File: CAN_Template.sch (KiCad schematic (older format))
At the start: 21 parts, among them U5 SN74LVC1T45DBVR, U6 SN65HVD1050D, U7 MCP2515-xSO, U8 SN74LVC1T45DBVR

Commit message: A very rough placement of components, some routing
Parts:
- removed D3: D5V0L2B3W-7, Package_TO_SOT_SMD:SOT-23, symbol Device:D_TVS_x2_CAA
- added D3: D_TVS_x2_AAC, Package_TO_SOT_SMD:SOT-23, symbol Device:D_TVS_x2_AAC
- C18, C19, C20, C21, C22, C23, C24, C25, C50, C51: footprint Capacitor_SMD:C_0805_2012Metric -> Capacitor_SMD:C_0603_1608Metric
- NP1, NP2, R12, R13, R14, R15: footprint Resistor_SMD:R_0805_2012Metric -> Resistor_SMD:R_0603_1608Metric
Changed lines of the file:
@@
 F 0 "NP1" H 8668 3446 50  0000 L CNN
 F 1 "60" H 8668 3355 50  0000 L CNN
-F 2 "Resistor_SMD:R_0805_2012Metric" V 8640 3390 50  0001 C CNN
+F 2 "Resistor_SMD:R_0603_1608Metric" V 8640 3390 50  0001 C CNN
 F 3 "~" H 8600 3400 50  0001 C CNN
 	1    8600 3400
@@
 F 0 "C19" V 7498 2850 50  0000 C CNN
 F 1 "1nf" V 7589 2850 50  0000 C CNN
-F 2 "Capacitor_SMD:C_0805_2012Metric" H 7788 2700 50  0001 C CNN
+F 2 "Capacitor_SMD:C_0603_1608Metric" H 7788 2700 50  0001 C CNN
 F 3 "~" H 7750 2850 50  0001 C CNN
 	1    7750 2850
@@
 F 0 "C21" V 7650 2850 50  0000 C CNN
 F 1 "100nf" V 7589 3050 50  0000 C CNN
-F 2 "Capacitor_SMD:C_0805_2012Metric" H 7788 2900 50  0001 C CNN
+F 2 "Capacitor_SMD:C_0603_1608Metric" H 7788 2900 50  0001 C CNN
 F 3 "~" H 7750 3050 50  0001 C CNN
 	1    7750 3050
@@
 F 0 "C24" H 8715 4346 50  0000 L CNN
 F 1 "100pf" H 8715 4255 50  0000 L CNN
-F 2 "Capacitor_SMD:C_0805_2012Metric" H 8638 4150 50  0001 C CNN
+F 2 "Capacitor_SMD:C_0603_1608Metric" H 8638 4150 50  0001 C CNN
 F 3 "~" H 8600 4300 50  0001 C CNN
 	1    8600 4300
@@
 F 0 "NP2" H 8668 3846 50  0000 L CNN
 F 1 "60" H 8668 3755 50  0000 L CNN
-F 2 "Resistor_SMD:R_0805_2012Metric" V 8640 3790 50  0001 C CNN
+F 2 "Resistor_SMD:R_0603_1608Metric" V 8640 3790 50  0001 C CNN
 F 3 "~" H 8600 3800 50  0001 C CNN
 	1    8600 3800
@@
 F 0 "C23" H 9015 3646 50  0000 L CNN
 F 1 "1nf" H 9015 3555 50  0000 L CNN
-F 2 "Capacitor_SMD:C_0805_2012Metric" H 8938 3450 50  0001 C CNN
+F 2 "Capacitor_SMD:C_0603_1608Metric" H 8938 3450 50  0001 C CNN
 F 3 "~" H 8900 3600 50  0001 C CNN
 	1    8900 3600
@@
 F 0 "R13" H 8368 3646 50  0000 L CNN
 F 1 "0" H 8368 3555 50  0000 L CNN
-F 2 "Resistor_SMD:R_0805_2012Metric" V 8340 3590 50  0001 C CNN
+F 2 "Resistor_SMD:R_0603_1608Metric" V 8340 3590 50  0001 C CNN
 F 3 "~" H 8300 3600 50  0001 C CNN
 	1    8300 3600
 	0    -1   -1   0
-$EndComp
-$Comp
-L Device:D_TVS_x2_CAA D3
-U 1 1 5DD0169A
-P 9350 3600
-F 0 "D3" V 9304 3679 50  0000 L CNN
-F 1 "D5V0L2B3W-7" V 9395 3679 50  0000 L CNN
-F 2 "Package_TO_SOT_SMD:SOT-23" H 9200 3600 50  0001 C CNN
-F 3 "https://www.mouser.com/datasheet/2/115/D5V0L2B3W-218988.pdf" H 9200 3600 50  0001 C CNN
-	1    9350 3600
-	0    1    1    0
 $EndComp
 $Comp
@@
 F 0 "R14" H 6918 4096 50  0000 L CNN
 F 1 "10k" H 6918 4005 50  0000 L CNN
-F 2 "Resistor_SMD:R_0805_2012Metric" V 6890 4040 50  0001 C CNN
+F 2 "Resistor_SMD:R_0603_1608Metric" V 6890 4040 50  0001 C CNN
 F 3 "~" H 6850 4050 50  0001 C CNN
 	1    6850 4050
@@
 F 0 "R12" H 3918 2996 50  0000 L CNN
 F 1 "0" H 3918 2905 50  0000 L CNN
-F 2 "Resistor_SMD:R_0805_2012Metric" V 3890 2940 50  0001 C CNN
+F 2 "Resistor_SMD:R_0603_1608Metric" V 3890 2940 50  0001 C CNN
 F 3 "~" H 3850 2950 50  0001 C CNN
 	1    3850 2950
@@
 F 0 "C20" H 8715 2946 50  0000 L CNN
 F 1 "100pf" H 8715 2855 50  0000 L CNN
-F 2 "Capacitor_SMD:C_0805_2012Metric" H 8638 2750 50  0001 C CNN
+F 2 "Capacitor_SMD:C_0603_1608Metric" H 8638 2750 50  0001 C CNN
 F 3 "~" H 8600 2900 50  0001 C CNN
 	1    8600 2900
@@
 F 0 "C51" V 2248 5000 50  0000 C CNN
 F 1 "1nf" V 2339 5000 50  0000 C CNN
-F 2 "Capacitor_SMD:C_0805_2012Metric" H 2538 4850 50  0001 C CNN
+F 2 "Capacitor_SMD:C_0603_1608Metric" H 2538 4850 50  0001 C CNN
 F 3 "~" H 2500 5000 50  0001 C CNN
 	1    2500 5000
@@
 F 0 "C50" V 2400 4600 50  0000 C CNN
 F 1 "100nf" V 2339 4800 50  0000 C CNN
-F 2 "Capacitor_SMD:C_0805_2012Metric" H 2538 4650 50  0001 C CNN
+F 2 "Capacitor_SMD:C_0603_1608Metric" H 2538 4650 50  0001 C CNN
 F 3 "~" H 2500 4800 50  0001 C CNN
 	1    2500 4800
@@
 F 0 "C18" V 4300 2800 50  0000 C CNN
 F 1 "100pf" V 3989 2800 50  0000 C CNN
-F 2 "Capacitor_SMD:C_0805_2012Metric" H 4188 2650 50  0001 C CNN
+F 2 "Capacitor_SMD:C_0603_1608Metric" H 4188 2650 50  0001 C CNN
 F 3 "~" H 4150 2800 50  0001 C CNN
 	1    4150 2800
@@
 F 0 "C22" H 6892 3196 50  0000 L CNN
 F 1 "100pF" H 6892 3105 50  0000 L CNN
-F 2 "Capacitor_SMD:C_0805_2012Metric" H 6800 3150 50  0001 C CNN
+F 2 "Capacitor_SMD:C_0603_1608Metric" H 6800 3150 50  0001 C CNN
 F 3 "~" H 6800 3150 50  0001 C CNN
 	1    6800 3150
@@
 F 0 "C25" V 5900 4450 50  0000 C CNN
 F 1 "100pf" V 5589 4450 50  0000 C CNN
-F 2 "Capacitor_SMD:C_0805_2012Metric" H 5788 4300 50  0001 C CNN
+F 2 "Capacitor_SMD:C_0603_1608Metric" H 5788 4300 50  0001 C CNN
 F 3 "~" H 5750 4450 50  0001 C CNN
 	1    5750 4450
@@
 F 0 "R15" H 6118 4346 50  0000 L CNN
 F 1 "0" H 6118 4255 50  0000 L CNN
-F 2 "Resistor_SMD:R_0805_2012Metric" V 6090 4290 50  0001 C CNN
+F 2 "Resistor_SMD:R_0603_1608Metric" V 6090 4290 50  0001 C CNN
 F 3 "~" H 6050 4300 50  0001 C CNN
 	1    6050 4300
@@
 	-1   0    0    1
 $EndComp
+$Comp
+L Device:D_TVS_x2_AAC D3
+U 1 1 5E29CE34
+P 9350 3600
+F 0 "D3" V 9304 3679 50  0000 L CNN
+F 1 "D_TVS_x2_AAC" V 9395 3679 50  0000 L CNN
+F 2 "Package_TO_SOT_SMD:SOT-23" H 9200 3600 50  0001 C CNN
+F 3 "~" H 9200 3600 50  0001 C CNN
+	1    9350 3600
+	0    1    1    0
+$EndComp
 $EndSCHEMATC

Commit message: Fixed caps and added grounding
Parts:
- U5, U8: symbol dk_Logic-Translators-Level-Shifters:SN74LVC1T45DBVR -> MASA-Radio-Board-rescue:SN74LVC1T45DBVR-dk_Logic-Translators-Level-Shifters
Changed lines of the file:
@@
 EESchema Schematic File Version 4
+LIBS:MASA-Radio Board-cache
 EELAYER 30 0
 EELAYER END
@@
 	6800 3050 6800 2950
 $Comp
-L dk_Logic-Translators-Level-Shifters:SN74LVC1T45DBVR U5
+L MASA-Radio-Board-rescue:SN74LVC1T45DBVR-dk_Logic-Translators-Level-Shifters U5
 U 1 1 5E23BA35
 P 5250 2950
+AR Path="/5E23BA35" Ref="U5"  Part="1"
+AR Path="/5E22EDDC/5E23BA35" Ref="U5"  Part="1"
 F 0 "U5" H 5250 2347 60  0000 C CNN
 F 1 "SN74LVC1T45DBVR" H 5250 2453 60  0000 C CNN
@@
 $EndComp
 $Comp
-L dk_Logic-Translators-Level-Shifters:SN74LVC1T45DBVR U8
+L MASA-Radio-Board-rescue:SN74LVC1T45DBVR-dk_Logic-Translators-Level-Shifters U8
 U 1 1 5E2400EF
 P 5250 4300
+AR Path="/5E2400EF" Ref="U8"  Part="1"
+AR Path="/5E22EDDC/5E2400EF" Ref="U8"  Part="1"
 F 0 "U8" H 5250 3697 60  0000 C CNN
 F 1 "SN74LVC1T45DBVR" H 5250 3803 60  0000 C CNN

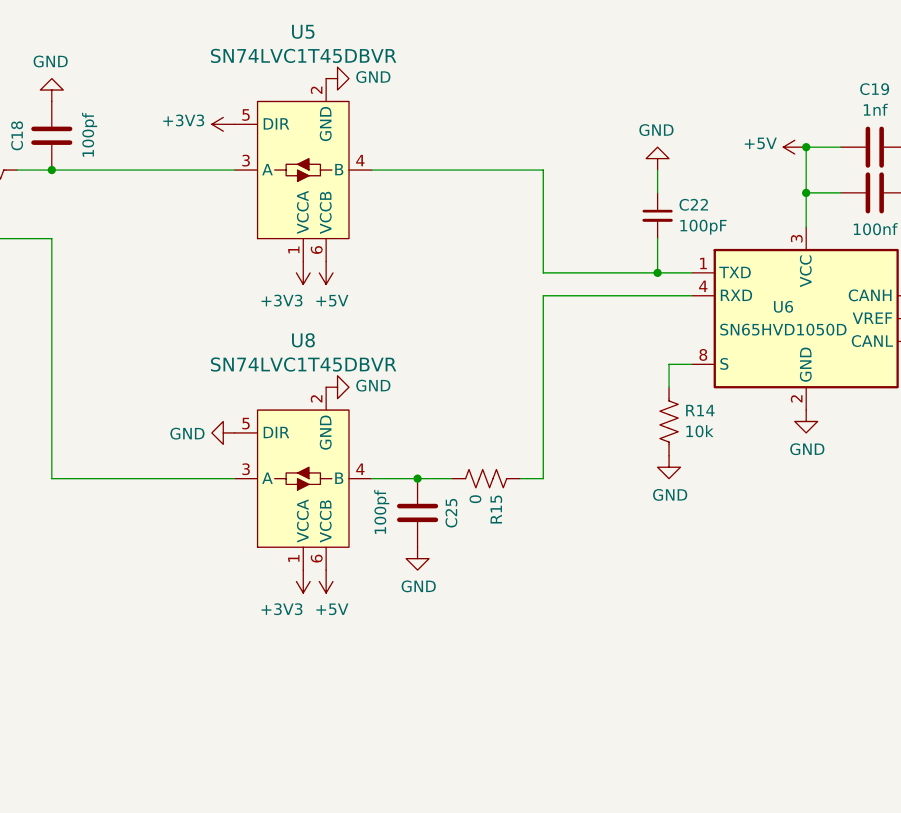
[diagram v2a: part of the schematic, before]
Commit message: Added filters and connected missing analog lines. Also fixed USB
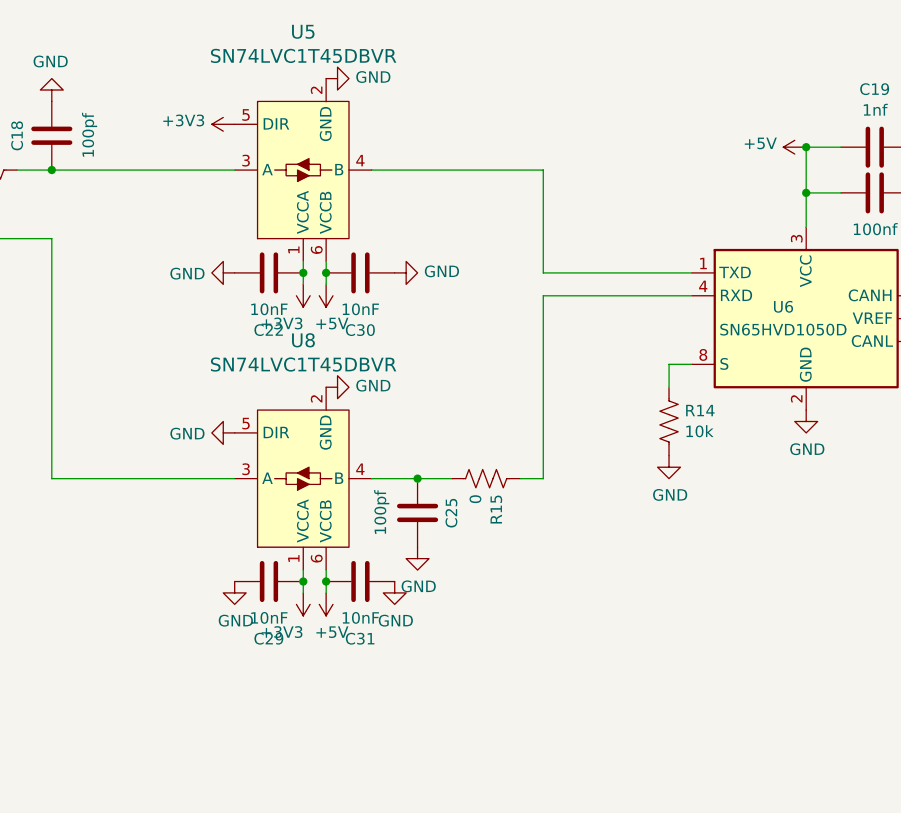
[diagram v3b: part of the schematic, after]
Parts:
- removed C22: 100pF, Capacitor_SMD:C_0603_1608Metric, symbol Device:C_Small
- added C22, C29, C30, C31: 10nF, Capacitor_SMD:C_0603_1608Metric, symbol Device:C
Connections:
- net +3V3: now also C22.2, C29.2
- net +5V: now also C30.1, C31.1
- net GND: now also C22.1, C29.1, C30.2, C31.2
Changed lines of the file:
@@
 CAN_Transciever
-$Comp
-L Device:C_Small C22
-U 1 1 5E22EBAC
-P 6800 3150
-F 0 "C22" H 6892 3196 50  0000 L CNN
-F 1 "100pF" H 6892 3105 50  0000 L CNN
-F 2 "Capacitor_SMD:C_0603_1608Metric" H 6800 3150 50  0001 C CNN
-F 3 "~" H 6800 3150 50  0001 C CNN
-	1    6800 3150
-	1    0    0    -1
-$EndComp
-Wire Wire Line
-	6950 3400 6800 3400
-Wire Wire Line
-	6800 3400 6800 3250
-$Comp
-L power:GND #PWR056
-U 1 1 5E231658
-P 6800 2950
-F 0 "#PWR056" H 6800 2700 50  0001 C CNN
-F 1 "GND" H 6805 2777 50  0000 C CNN
-F 2 "" H 6800 2950 50  0001 C CNN
-F 3 "" H 6800 2950 50  0001 C CNN
-	1    6800 2950
-	-1   0    0    1
-$EndComp
-Wire Wire Line
-	6800 3050 6800 2950
 $Comp
 L MASA-Radio-Board-rescue:SN74LVC1T45DBVR-dk_Logic-Translators-Level-Shifters U5
@@
 	0    -1   -1   0
 $EndComp
-Wire Wire Line
-	6800 3400 6300 3400
-Connection ~ 6800 3400
 $Comp
 L power:+3V3 #PWR052
@@
 L power:+3V3 #PWR059
 U 1 1 5E266276
-P 5250 3350
-F 0 "#PWR059" H 5250 3200 50  0001 C CNN
-F 1 "+3V3" H 5344 3523 50  0000 C CNN
-F 2 "" H 5250 3350 50  0001 C CNN
-F 3 "" H 5250 3350 50  0001 C CNN
-	1    5250 3350
+P 5250 3450
+F 0 "#PWR059" H 5250 3300 50  0001 C CNN
+F 1 "+3V3" H 5344 3623 50  0000 C CNN
+F 2 "" H 5250 3450 50  0001 C CNN
+F 3 "" H 5250 3450 50  0001 C CNN
+	1    5250 3450
 	-1   0    0    1
 $EndComp
@@
 L power:+5V #PWR060
 U 1 1 5E2667FA
-P 5350 3350
-F 0 "#PWR060" H 5350 3200 50  0001 C CNN
-F 1 "+5V" H 5326 3523 50  0000 C CNN
-F 2 "" H 5350 3350 50  0001 C CNN
-F 3 "" H 5350 3350 50  0001 C CNN
-	1    5350 3350
+P 5350 3450
+F 0 "#PWR060" H 5350 3300 50  0001 C CNN
+F 1 "+5V" H 5326 3623 50  0000 C CNN
+F 2 "" H 5350 3450 50  0001 C CNN
+F 3 "" H 5350 3450 50  0001 C CNN
+	1    5350 3450
 	-1   0    0    1
 $EndComp
@@
 L power:+5V #PWR069
 U 1 1 5E267CFB
-P 5350 4700
-F 0 "#PWR069" H 5350 4550 50  0001 C CNN
-F 1 "+5V" H 5326 4873 50  0000 C CNN
-F 2 "" H 5350 4700 50  0001 C CNN
-F 3 "" H 5350 4700 50  0001 C CNN
-	1    5350 4700
+P 5350 4800
+F 0 "#PWR069" H 5350 4650 50  0001 C CNN
+F 1 "+5V" H 5326 4973 50  0000 C CNN
+F 2 "" H 5350 4800 50  0001 C CNN
+F 3 "" H 5350 4800 50  0001 C CNN
+	1    5350 4800
 	-1   0    0    1
 $EndComp
@@
 L power:+3V3 #PWR068
 U 1 1 5E267CF5
-P 5250 4700
-F 0 "#PWR068" H 5250 4550 50  0001 C CNN
-F 1 "+3V3" H 5344 4873 50  0000 C CNN
-F 2 "" H 5250 4700 50  0001 C CNN
-F 3 "" H 5250 4700 50  0001 C CNN
-	1    5250 4700
+P 5250 4800
+F 0 "#PWR068" H 5250 4650 50  0001 C CNN
+F 1 "+3V3" H 5344 4973 50  0000 C CNN
+F 2 "" H 5250 4800 50  0001 C CNN
+F 3 "" H 5250 4800 50  0001 C CNN
+	1    5250 4800
 	-1   0    0    1
 $EndComp
@@
 	0    1    1    0
 $EndComp
+$Comp
+L Device:C C22
+U 1 1 5E2F1379
+P 5100 3400
+F 0 "C22" V 4848 3400 50  0000 C CNN
+F 1 "10nF" V 4939 3400 50  0000 C CNN
+F 2 "Capacitor_SMD:C_0603_1608Metric" H 5138 3250 50  0001 C CNN
+F 3 "~" H 5100 3400 50  0001 C CNN
+	1    5100 3400
+	0    -1   -1   0
+$EndComp
+$Comp
+L power:GND #PWR0102
+U 1 1 5E2F2685
+P 4950 3400
+F 0 "#PWR0102" H 4950 3150 50  0001 C CNN
+F 1 "GND" V 4955 3272 50  0000 R CNN
+F 2 "" H 4950 3400 50  0001 C CNN
+F 3 "" H 4950 3400 50  0001 C CNN
+	1    4950 3400
+	0    1    1    0
+$EndComp
+$Comp
+L Device:C C30
+U 1 1 5E2F2CA8
+P 5500 3400
+F 0 "C30" V 5248 3400 50  0000 C CNN
+F 1 "10nF" V 5339 3400 50  0000 C CNN
+F 2 "Capacitor_SMD:C_0603_1608Metric" H 5538 3250 50  0001 C CNN
+F 3 "~" H 5500 3400 50  0001 C CNN
+	1    5500 3400
+	0    -1   -1   0
+$EndComp
+$Comp
+L power:GND #PWR0103
+U 1 1 5E2F3088
+P 5650 3400
+F 0 "#PWR0103" H 5650 3150 50  0001 C CNN
+F 1 "GND" V 5655 3272 50  0000 R CNN
+F 2 "" H 5650 3400 50  0001 C CNN
+F 3 "" H 5650 3400 50  0001 C CNN
+	1    5650 3400
+	0    -1   -1   0
+$EndComp
+Wire Wire Line
+	5350 3350 5350 3400
+Connection ~ 5350 3400
+Wire Wire Line
+	5350 3400 5350 3450
+Wire Wire Line
+	5250 3450 5250 3400
+Connection ~ 5250 3400
+Wire Wire Line
+	5250 3400 5250 3350
+$Comp
+L Device:C C29
+U 1 1 5E2F68DA
+P 5100 4750
+F 0 "C29" V 4848 4750 50  0000 C CNN
+F 1 "10nF" V 4939 4750 50  0000 C CNN
+F 2 "Capacitor_SMD:C_0603_1608Metric" H 5138 4600 50  0001 C CNN
+F 3 "~" H 5100 4750 50  0001 C CNN
+	1    5100 4750
+	0    -1   -1   0
+$EndComp
+$Comp
+L Device:C C31
+U 1 1 5E2F6921
+P 5500 4750
+F 0 "C31" V 5248 4750 50  0000 C CNN
+F 1 "10nF" V 5339 4750 50  0000 C CNN
+F 2 "Capacitor_SMD:C_0603_1608Metric" H 5538 4600 50  0001 C CNN
+F 3 "~" H 5500 4750 50  0001 C CNN
+	1    5500 4750
+	0    -1   -1   0
+$EndComp
+$Comp
+L power:GND #PWR0104
+U 1 1 5E2F6DA7
+P 5650 4750
+F 0 "#PWR0104" H 5650 4500 50  0001 C CNN
+F 1 "GND" H 5655 4577 50  0000 C CNN
+F 2 "" H 5650 4750 50  0001 C CNN
+F 3 "" H 5650 4750 50  0001 C CNN
+	1    5650 4750
+	1    0    0    -1
+$EndComp
+$Comp
+L power:GND #PWR0105
+U 1 1 5E2F7012
+P 4950 4750
+F 0 "#PWR0105" H 4950 4500 50  0001 C CNN
+F 1 "GND" H 4955 4577 50  0000 C CNN
+F 2 "" H 4950 4750 50  0001 C CNN
+F 3 "" H 4950 4750 50  0001 C CNN
+	1    4950 4750
+	1    0    0    -1
+$EndComp
+Wire Wire Line
+	5250 4800 5250 4750
+Connection ~ 5250 4750
+Wire Wire Line
+	5250 4750 5250 4700
+Wire Wire Line
+	5350 4700 5350 4750
+Connection ~ 5350 4750
+Wire Wire Line
+	5350 4750 5350 4800
+Wire Wire Line
+	6300 3400 6950 3400
 $EndSCHEMATC

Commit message: Added 0 Ohm resistors
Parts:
- added R19, R20: 0, Resistor_SMD:R_0603_1608Metric, symbol Device:R_US
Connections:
- net +3V3: now also R19.1; no longer C50.1, C51.2, U7.9 (VSS)
- net +5V: now also R20.2; no longer C19.2, C21.1, U6.3 (VCC)
- new net: C50.1, C51.2, R19.2, U7.9 (VSS)
- new net: C19.2, C21.1, R20.1, U6.3 (VCC)
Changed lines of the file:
@@
 L power:+5V #PWR054
 U 1 1 5E0A2EDD
-P 7450 2850
-F 0 "#PWR054" H 7450 2700 50  0001 C CNN
-F 1 "+5V" V 7465 2978 50  0000 L CNN
-F 2 "" H 7450 2850 50  0001 C CNN
-F 3 "" H 7450 2850 50  0001 C CNN
-	1    7450 2850
+P 7150 2850
+F 0 "#PWR054" H 7150 2700 50  0001 C CNN
+F 1 "+5V" V 7165 2978 50  0000 L CNN
+F 2 "" H 7150 2850 50  0001 C CNN
+F 3 "" H 7150 2850 50  0001 C CNN
+	1    7150 2850
 	0    -1   -1   0
 $EndComp
@@
 L power:+3V3 #PWR072
 U 1 1 5E269EEC
-P 2800 5000
-F 0 "#PWR072" H 2800 4850 50  0001 C CNN
-F 1 "+3V3" V 2815 5128 50  0000 L CNN
-F 2 "" H 2800 5000 50  0001 C CNN
-F 3 "" H 2800 5000 50  0001 C CNN
-	1    2800 5000
+P 3100 5000
+F 0 "#PWR072" H 3100 4850 50  0001 C CNN
+F 1 "+3V3" V 3115 5128 50  0000 L CNN
+F 2 "" H 3100 5000 50  0001 C CNN
+F 3 "" H 3100 5000 50  0001 C CNN
+	1    3100 5000
 	0    1    1    0
 $EndComp
@@
 Wire Wire Line
 	6300 3400 6950 3400
+$Comp
+L Device:R_US R19
+U 1 1 5E365C9D
+P 2950 5000
+F 0 "R19" H 3018 5046 50  0000 L CNN
+F 1 "0" H 3018 4955 50  0000 L CNN
+F 2 "Resistor_SMD:R_0603_1608Metric" V 2990 4990 50  0001 C CNN
+F 3 "~" H 2950 5000 50  0001 C CNN
+	1    2950 5000
+	0    1    1    0
+$EndComp
+$Comp
+L Device:R_US R20
+U 1 1 5E36C8CF
+P 7300 2850
+F 0 "R20" H 7368 2896 50  0000 L CNN
+F 1 "0" H 7368 2805 50  0000 L CNN
+F 2 "Resistor_SMD:R_0603_1608Metric" V 7340 2840 50  0001 C CNN
+F 3 "~" H 7300 2850 50  0001 C CNN
+	1    7300 2850
+	0    1    1    0
+$EndComp
 $EndSCHEMATC
